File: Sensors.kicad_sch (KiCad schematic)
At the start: 6 parts, among them U3 MCP9700AT-ETT

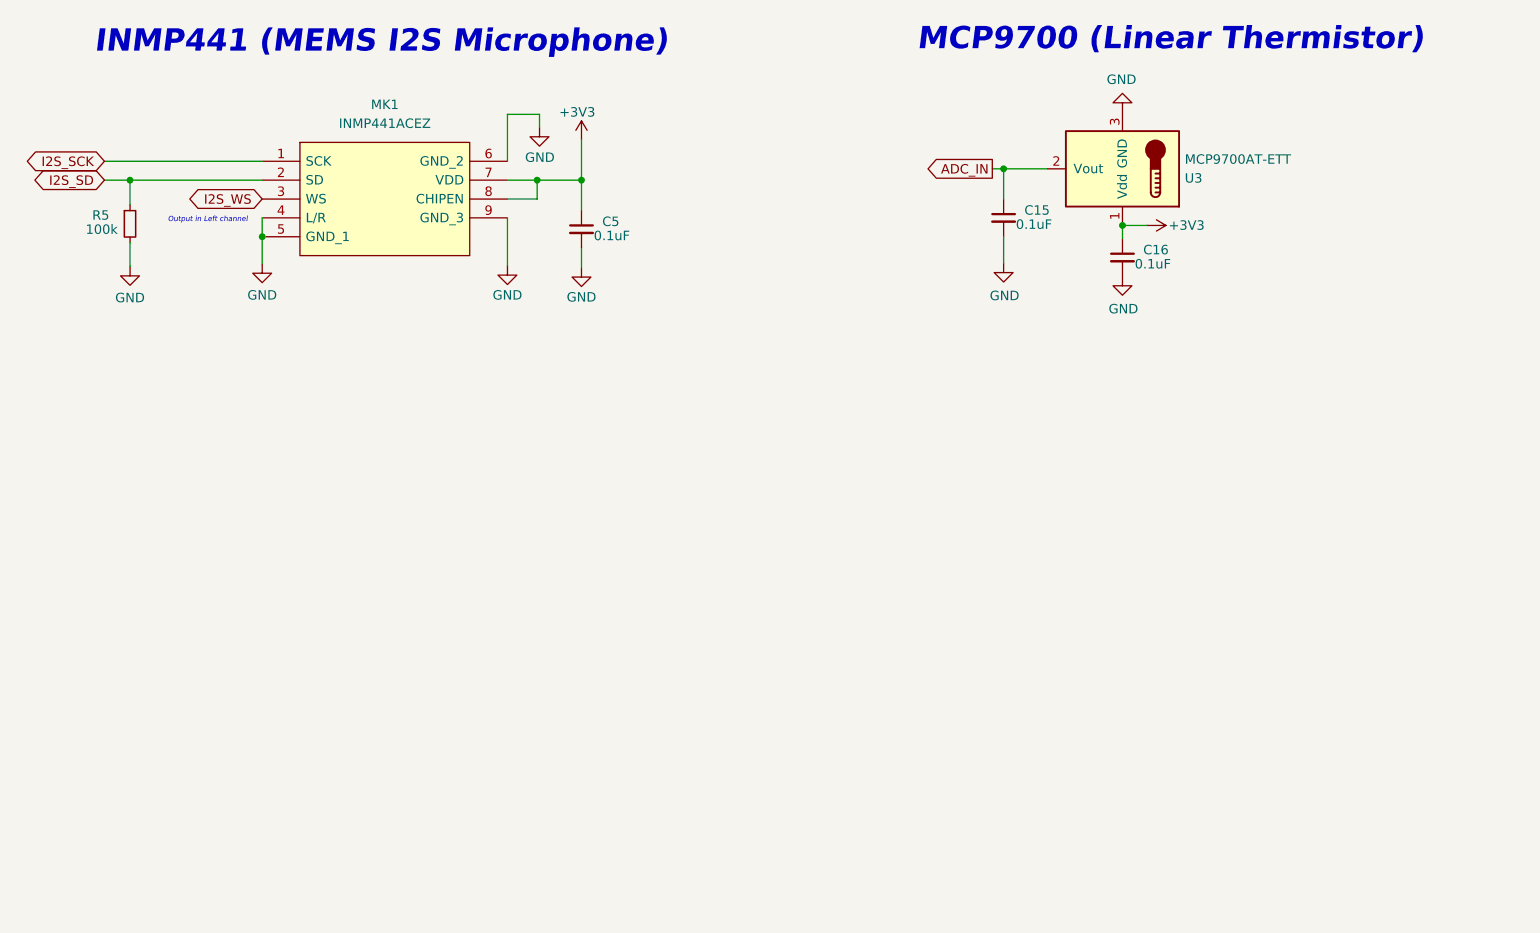
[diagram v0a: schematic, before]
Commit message: Added accelerometer
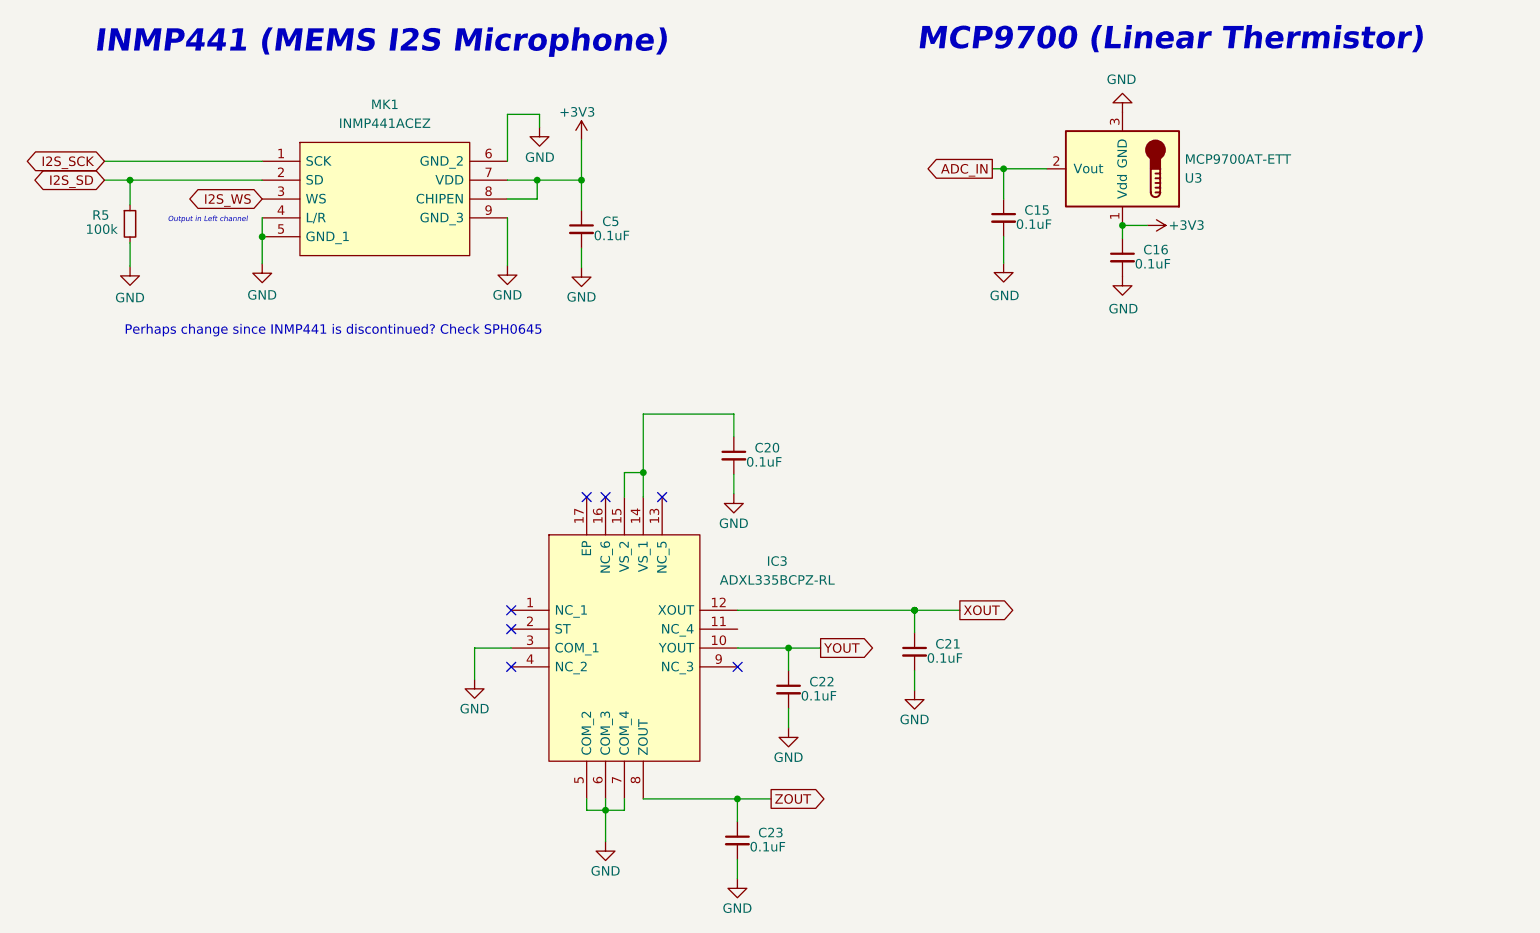
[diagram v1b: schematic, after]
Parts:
- added C20, C21, C22, C23: 0.1uF, Capacitor_SMD:C_0402_1005Metric, symbol Device:C_Small
- added IC3: ADXL335BCPZ-RL, Package_CSP:LFCSP-16-1EP_4x4mm_P0.65mm_EP2.1x2.1mm, symbol ADXL335BCPZ-RL:ADXL335BCPZ-RL
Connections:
- net GND: now also C20.2, C21.2, C22.2, C23.2, IC3.3 (COM_1), IC3.5 (COM_2), IC3.6 (COM_3), IC3.7 (COM_4)
- new net: C20.1, IC3.14 (VS_1), IC3.15 (VS_2)
- new net XOUT: C21.1, IC3.12 (XOUT)
- new net YOUT: C22.1, IC3.10 (YOUT)
- new net ZOUT: C23.1, IC3.8 (ZOUT)
- no-connect marks 0 -> 7
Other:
- note added: "Perhaps change since INMP441 is discontinued? Check SPH0645"

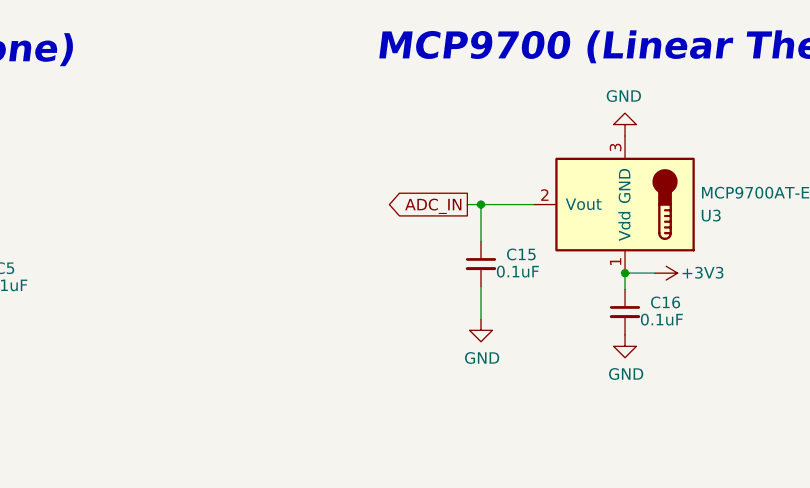
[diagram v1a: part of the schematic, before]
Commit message: Made new layout
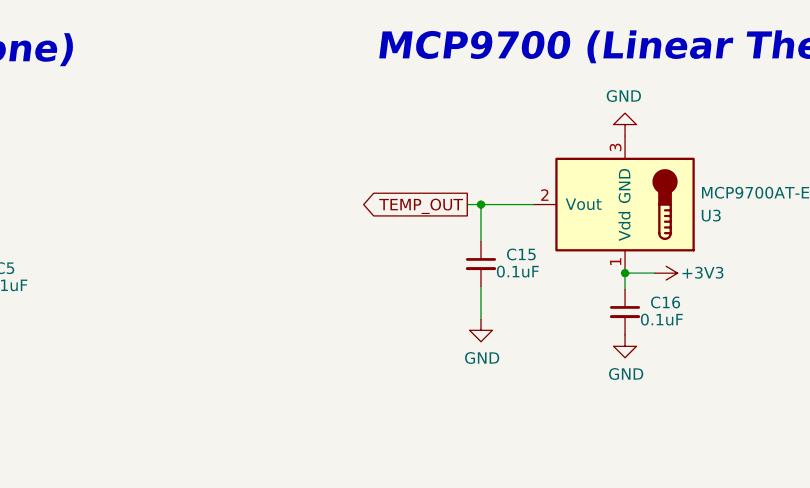
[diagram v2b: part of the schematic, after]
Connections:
- net ADC_IN renamed TEMP_OUT
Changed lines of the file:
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@@
     )
   )
-  (global_label "ADC_IN" (shape output) (at 180.086 85.344 180) (fields_autoplaced)
+  (global_label "TEMP_OUT" (shape output) (at 180.086 85.344 180) (fields_autoplaced)
     (effects (font (size 1.27 1.27)) (justify right))
-    (property "Intersheet References" "${INTERSHEET_REFS}" (id 0) (at 171.2304 85.2646 0)
+    (property "Intersheet References" "${INTERSHEET_REFS}" (id 0) (at 168.3275 85.2646 0)
       (effects (font (size 1.27 1.27)) (justify right) hide)
     )
